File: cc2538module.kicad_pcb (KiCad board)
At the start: 4 copper layers, 24.4 x 27.6 mm, 68 parts, among them J1 XBEE_with_jtag, SW1 SW_PUSH, SW2 SW_PUSH, U1 CC2538, U2 TPS6273X, Y1 Crystal_GND24, Y2 Crystal

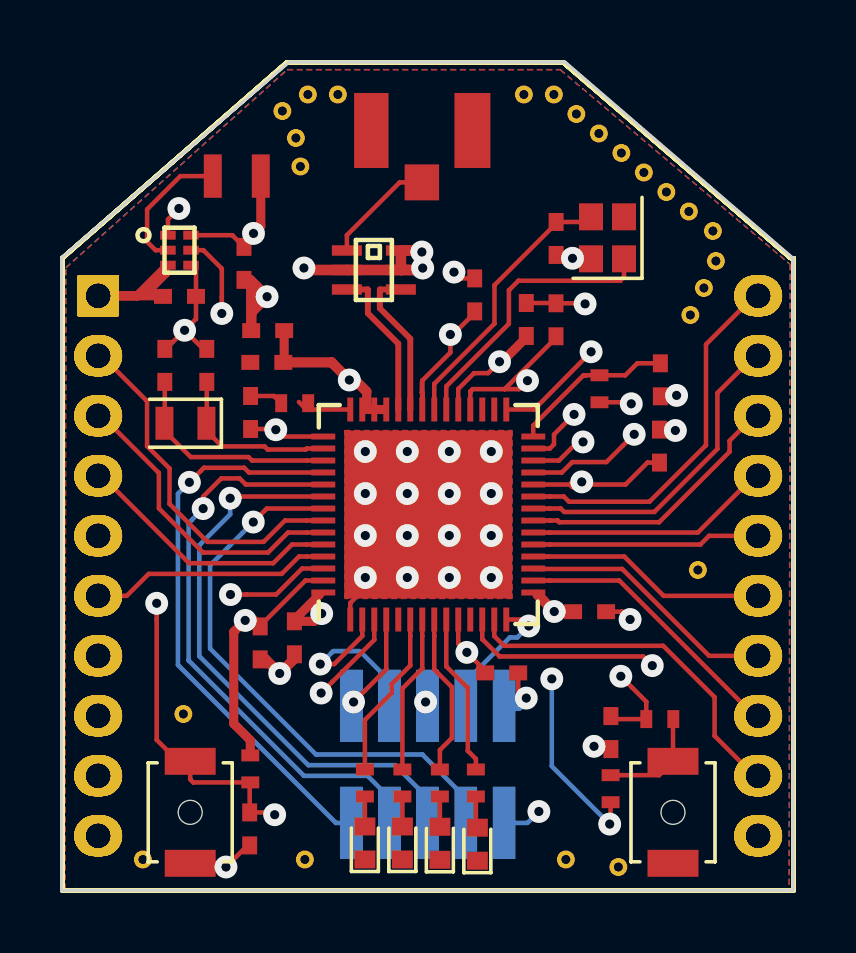
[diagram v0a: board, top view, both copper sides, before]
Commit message: Added C5 to PCB and rearrange the step down power converter as described in its datasheet
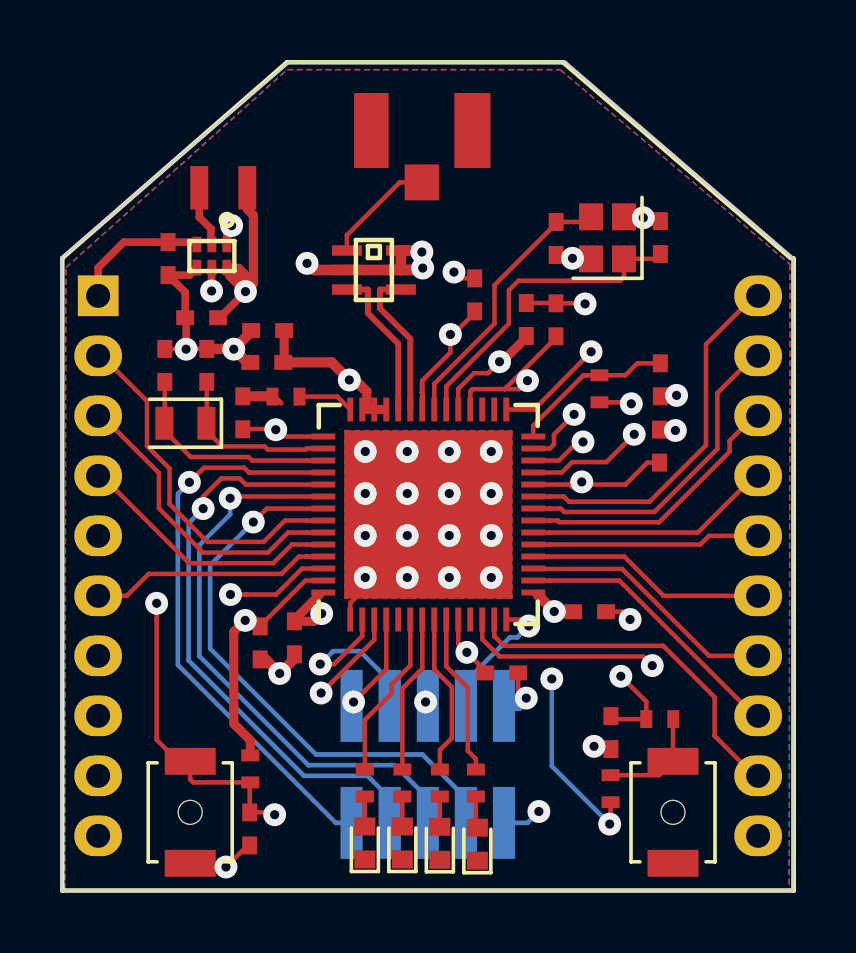
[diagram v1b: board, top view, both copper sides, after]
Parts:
- removed the J1 at (90.6, 65.1) (x3)
- removed REF** (x23): VIA-0.6mm, SensorsUnleashed:VIA-0.6mm
- added C5: 12pF, Capacitors_SMD:C_0402_NoSilk, F.Cu at (98.3, 57.1)
- C1: value 1n -> 1nF
- C13, C14, C16, C17, C18, C19: value 100n -> 100nF
- C2, C4: value 1u -> 1uF
- C20: value 220p -> 220pF
- C6: value 12p -> 12pF
- C8, C9: value 22p -> 22pF
- LED2: value Yellow -> Amber
- R2: value R -> 1k
- R6, R7, R8, R9: value 680R -> 100R
- moved C10 2.29 mm to (83.1, 59.8), turned to 180 degrees
- moved C11 1.32 mm to (81.9, 57.8), turned to 270 degrees
- moved U2 1.10 mm to (83.4, 57.7), turned to 270 degrees
- moved L1 0.60 mm to (83.8, 55.5)
- moved R3 0.36 mm to (85.9, 62.4)
- moved C18 0.26 mm to (84.4, 63.0)
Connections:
- net PA0/DIO0 renamed PA0/DIO7
- net PA1/DIO1 renamed PA1/DIO6
- net PA2/DIO2 renamed PA2/DIO5
- net PA3/DIO3 renamed PA3/DIO4
- net PA4/DIO4 renamed PA4/DIO3
- net PA5/DIO5 renamed PA5/DIO2
- net PA6/DIO6 renamed PA6/DIO1
- net PA7/DIO7 renamed PA7/DIO0
- net PB0/STAT renamed PD3/STAT
- net PC3/DIO10 renamed PD2/DIO10
- net PC4/L0 renamed PC7/L0
- net PC5/L1 renamed PC6/L1
- net PC6/L2 renamed PC5/L2
- net PC7/L3 renamed PC4/L3
- net USER_BUTTON renamed PD0/USER_BUTTON
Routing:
- net XBEE_VDD: track 7.84 -> 4.61 mm
- net Net-(L1-Pad1): track 4.54 -> 2.06 mm
- net VDD: track 89.8 -> 92.3 mm
- net PD3/STAT: track 20.4 -> 18.1 mm
- net GND: track 51.5 -> 53.0 mm, vias 31 -> 32
- net Net-(C5-Pad1): track 9.46 -> 10.7 mm
- net PB1/ON/BYP: track 17.0 -> 15.9 mm

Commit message: New footprint and various small changes. PCB ordered at DirtyPCB 20170328
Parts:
- added REF**: VIA-0.6mm, SensorsUnleashed:VIA-0.6mm, F.Cu at (87.9, 60.5)
- added REF**: VIA-0.6mm, SensorsUnleashed:VIA-0.6mm, F.Cu at (81.4, 78.3)
- added REF**: VIA-0.6mm, SensorsUnleashed:VIA-0.6mm, F.Cu at (86.7, 78.3)
- added REF**: VIA-0.6mm, SensorsUnleashed:VIA-0.6mm, F.Cu at (85.9, 78.3)
- added REF**: VIA-0.6mm, SensorsUnleashed:VIA-0.6mm, F.Cu at (85.1, 78.3)
- added REF**: VIA-0.6mm, SensorsUnleashed:VIA-0.6mm, F.Cu at (94.1, 78.3)
- added REF**: VIA-0.6mm, SensorsUnleashed:VIA-0.6mm, F.Cu at (94.9, 78.3)
- added REF**: VIA-0.6mm, SensorsUnleashed:VIA-0.6mm, F.Cu at (95.7, 78.3)
- added REF**: VIA-0.6mm, SensorsUnleashed:VIA-0.6mm, F.Cu at (96.5, 78.3)
- added REF**: VIA-0.6mm, SensorsUnleashed:VIA-0.6mm, F.Cu at (97.3, 78.3)
- added REF**: VIA-0.6mm, SensorsUnleashed:VIA-0.6mm, F.Cu at (95.6, 74.6)
- added REF**: VIA-0.6mm, SensorsUnleashed:VIA-0.6mm, F.Cu at (81.4, 72.7)
- added REF**: VIA-0.6mm, SensorsUnleashed:VIA-0.6mm, F.Cu at (99.8, 71.4)
- added REF**: VIA-0.6mm, SensorsUnleashed:VIA-0.6mm, F.Cu at (98.9, 61.2)
- added REF**: VIA-0.6mm, SensorsUnleashed:VIA-0.6mm, F.Cu at (86.5, 58.2)
- added REF**: VIA-0.6mm, SensorsUnleashed:VIA-0.6mm, F.Cu at (85.7, 58.2)
- added REF**: VIA-0.6mm, SensorsUnleashed:VIA-0.6mm, F.Cu at (85.7, 56.5)
- added REF**: VIA-0.6mm, SensorsUnleashed:VIA-0.6mm, F.Cu at (85.5, 55.7)
- added REF**: VIA-0.6mm, SensorsUnleashed:VIA-0.6mm, F.Cu at (85.2, 55.0)
- added REF**: VIA-0.6mm, SensorsUnleashed:VIA-0.6mm, F.Cu at (84.8, 54.3)
- added REF**: VIA-0.6mm, SensorsUnleashed:VIA-0.6mm, F.Cu at (83.7, 54.1)
- added REF**: VIA-0.6mm, SensorsUnleashed:VIA-0.6mm, F.Cu at (84.4, 53.6)
- added REF**: VIA-0.6mm, SensorsUnleashed:VIA-0.6mm, F.Cu at (81.4, 73.5)
- added REF**: VIA-0.6mm, SensorsUnleashed:VIA-0.6mm, F.Cu at (85.0, 53.0)
- added REF**: VIA-0.6mm, SensorsUnleashed:VIA-0.6mm, F.Cu at (85.6, 52.5)
- added REF**: VIA-0.6mm, SensorsUnleashed:VIA-0.6mm, F.Cu at (99.0, 60.4)
- added REF**: VIA-0.6mm, SensorsUnleashed:VIA-0.6mm, F.Cu at (99.5, 59.8)
- added REF**: VIA-0.6mm, SensorsUnleashed:VIA-0.6mm, F.Cu at (100.0, 59.3)
- added REF**: VIA-0.6mm, SensorsUnleashed:VIA-0.6mm, F.Cu at (100.1, 58.5)
- added REF**: VIA-0.6mm, SensorsUnleashed:VIA-0.6mm, F.Cu at (100.6, 57.9)
- added REF**: VIA-0.6mm, SensorsUnleashed:VIA-0.6mm, F.Cu at (101.4, 57.6)
- added REF**: VIA-0.6mm, SensorsUnleashed:VIA-0.6mm, F.Cu at (100.8, 57.1)
- added REF**: VIA-0.6mm, SensorsUnleashed:VIA-0.6mm, F.Cu at (100.2, 56.6)
- added REF**: VIA-0.6mm, SensorsUnleashed:VIA-0.6mm, F.Cu at (81.4, 75.9)
- added REF**: VIA-0.6mm, SensorsUnleashed:VIA-0.6mm, F.Cu at (99.6, 56.1)
- added REF**: VIA-0.6mm, SensorsUnleashed:VIA-0.6mm, F.Cu at (99.0, 55.6)
- added REF**: VIA-0.6mm, SensorsUnleashed:VIA-0.6mm, F.Cu at (98.4, 55.1)
- added REF**: VIA-0.6mm, SensorsUnleashed:VIA-0.6mm, F.Cu at (97.8, 54.6)
- added REF**: VIA-0.6mm, SensorsUnleashed:VIA-0.6mm, F.Cu at (97.2, 54.1)
- added REF**: VIA-0.6mm, SensorsUnleashed:VIA-0.6mm, F.Cu at (96.6, 53.6)
- added REF**: VIA-0.6mm, SensorsUnleashed:VIA-0.6mm, F.Cu at (96.0, 53.1)
- added REF**: VIA-0.6mm, SensorsUnleashed:VIA-0.6mm, F.Cu at (95.4, 52.6)
- added REF**: VIA-0.6mm, SensorsUnleashed:VIA-0.6mm, F.Cu at (94.8, 52.0)
- added REF**: VIA-0.6mm, SensorsUnleashed:VIA-0.6mm, F.Cu at (94.1, 52.0)
- added REF**: VIA-0.6mm, SensorsUnleashed:VIA-0.6mm, F.Cu at (81.4, 76.7)
- added REF**: VIA-0.6mm, SensorsUnleashed:VIA-0.6mm, F.Cu at (93.3, 52.0)
- added REF**: VIA-0.6mm, SensorsUnleashed:VIA-0.6mm, F.Cu at (91.2, 52.0)
- added REF**: VIA-0.6mm, SensorsUnleashed:VIA-0.6mm, F.Cu at (90.4, 52.0)
- added REF**: VIA-0.6mm, SensorsUnleashed:VIA-0.6mm, F.Cu at (89.6, 52.0)
- added REF**: VIA-0.6mm, SensorsUnleashed:VIA-0.6mm, F.Cu at (87.8, 52.0)
- added REF**: VIA-0.6mm, SensorsUnleashed:VIA-0.6mm, F.Cu at (87.0, 52.0)
- added REF**: VIA-0.6mm, SensorsUnleashed:VIA-0.6mm, F.Cu at (86.2, 52.0)
- added REF**: VIA-0.6mm, SensorsUnleashed:VIA-0.6mm, F.Cu at (81.4, 77.5)
- added REF**: VIA-0.6mm, SensorsUnleashed:VIA-0.6mm, F.Cu at (79.0, 78.3)
- added REF**: VIA-0.6mm, SensorsUnleashed:VIA-0.6mm, F.Cu at (79.8, 78.3)
- added REF**: VIA-0.6mm, SensorsUnleashed:VIA-0.6mm, F.Cu at (80.6, 78.3)
- U1: footprint Housings_DFN_QFN:QFN-56-1EP_7x7mm_Pitch0.4mm -> SensorsUnleashed:cc2538_QFN_56
- moved C14 2.05 mm to (96.9, 65.6), turned to 0 degrees
- moved C1 1.90 mm to (96.6, 61.1), turned to 0 degrees
- moved C17 1.04 mm to (91.5, 59.8)
- moved L1 0.77 mm to (83.1, 55.8)
- moved C12 0.70 mm to (92.5, 72.1), turned to 270 degrees
- moved C4 0.67 mm to (85.5, 70.6)
- moved TR1 0.64 mm to (89.0, 58.8)
- moved U2 0.57 mm to (82.8, 57.7)
- moved R3 0.57 mm to (85.6, 61.9)
- moved C15 0.54 mm to (84.5, 70.6)
- moved C18 0.53 mm to (84.2, 62.5)
- moved C20 0.52 mm to (85.3, 60.8)
- moved C11 0.50 mm to (81.5, 58.0)
- moved C19 0.43 mm to (85.3, 59.8)
- moved C13 0.35 mm to (96.3, 69.7)
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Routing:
- net GND: track 53.0 -> 76.6 mm, vias 32 -> 31
- net VDD: track 92.3 -> 100.6 mm, vias 11 -> 10
- net TCK: track 19.4 -> 22.6 mm
- net Net-(C1-Pad1): track 5.46 -> 2.99 mm
- net PD3/STAT: track 18.1 -> 15.9 mm
- net PD1/DIO11: track 29.3 -> 31.5 mm
- net RF_N: track 5.12 -> 3.66 mm
- net RF_P: track 5.12 -> 3.69 mm
- net USB_N: track 7.10 -> 8.13 mm
- net PC1/DIO8: track 12.0 -> 11.2 mm
- net PB3/DIO13: track 8.97 -> 8.11 mm
- net Net-(C8-Pad1): track 5.80 -> 5.06 mm
- net Net-(AE1-Pad1): track 3.74 -> 4.35 mm
- net Net-(C9-Pad1): track 7.34 -> 6.73 mm
- net XBEE_VDD: track 4.61 -> 4.01 mm
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
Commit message: Rev B
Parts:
- removed C10, C11: 2.2uF, Capacitors_SMD:C_0402_NoSilk
- removed L1: 2.2uH, SensorsUnleashed:L_0805
- removed the REF** at (87.9, 60.5)
- removed the REF** at (81.4, 78.3)
- removed the REF** at (86.7, 78.3)
- removed the REF** at (85.9, 78.3)
- removed the REF** at (85.1, 78.3)
- removed the REF** at (94.1, 78.3)
- removed the REF** at (94.9, 78.3)
- removed the REF** at (95.7, 78.3)
- removed the REF** at (96.5, 78.3)
- removed the REF** at (97.3, 78.3)
- removed the REF** at (95.6, 74.6)
- removed the REF** at (81.4, 72.7)
- removed the REF** at (99.8, 71.4)
- removed the REF** at (98.9, 61.2)
- removed the REF** at (86.5, 58.2)
- removed the REF** at (85.7, 58.2)
- removed the REF** at (85.7, 56.5)
- removed the REF** at (85.5, 55.7)
- removed the REF** at (85.2, 55.0)
- removed the REF** at (84.8, 54.3)
- removed the REF** at (83.7, 54.1)
- removed the REF** at (84.4, 53.6)
- removed the REF** at (81.4, 73.5)
- removed the REF** at (85.0, 53.0)
- removed the REF** at (85.6, 52.5)
- removed the REF** at (99.0, 60.4)
- removed the REF** at (99.5, 59.8)
- removed the REF** at (100.0, 59.3)
- removed the REF** at (100.1, 58.5)
- removed the REF** at (100.6, 57.9)
- removed the REF** at (101.4, 57.6)
- removed the REF** at (100.8, 57.1)
- removed the REF** at (100.2, 56.6)
- removed the REF** at (81.4, 75.9)
- removed the REF** at (99.6, 56.1)
- removed the REF** at (99.0, 55.6)
- removed the REF** at (98.4, 55.1)
- removed the REF** at (97.8, 54.6)
- removed the REF** at (97.2, 54.1)
- removed the REF** at (96.6, 53.6)
- removed the REF** at (96.0, 53.1)
- removed the REF** at (95.4, 52.6)
- removed the REF** at (94.8, 52.0)
- removed the REF** at (94.1, 52.0)
- removed the REF** at (81.4, 76.7)
- removed the REF** at (93.3, 52.0)
- removed the REF** at (91.2, 52.0)
- removed the REF** at (90.4, 52.0)
- removed the REF** at (89.6, 52.0)
- removed the REF** at (87.8, 52.0)
- removed the REF** at (87.0, 52.0)
- removed the REF** at (86.2, 52.0)
- removed the REF** at (81.4, 77.5)
- removed the REF** at (79.0, 78.3)
- removed the REF** at (79.8, 78.3)
- removed the REF** at (80.6, 78.3)
- removed U2: TPS6273X, SensorsUnleashed:SON6
- added REF**: VIA-0.6mm, SensorsUnleashed:VIA-0.6mm, F.Cu at (87.3, 53.3)
- added REF**: VIA-0.6mm, SensorsUnleashed:VIA-0.6mm, F.Cu at (91.7, 56.9)
- added REF**: VIA-0.6mm, SensorsUnleashed:VIA-0.6mm, F.Cu at (101.0, 57.6)
- added REF**: VIA-0.6mm, SensorsUnleashed:VIA-0.6mm, F.Cu at (100.2, 56.8)
- added REF**: VIA-0.6mm, SensorsUnleashed:VIA-0.6mm, F.Cu at (99.3, 56.1)
- added REF**: VIA-0.6mm, SensorsUnleashed:VIA-0.6mm, F.Cu at (98.5, 55.3)
- added REF**: VIA-0.6mm, SensorsUnleashed:VIA-0.6mm, F.Cu at (97.6, 54.6)
- added REF**: VIA-0.6mm, SensorsUnleashed:VIA-0.6mm, F.Cu at (96.7, 53.8)
- added REF**: VIA-0.6mm, SensorsUnleashed:VIA-0.6mm, F.Cu at (95.9, 53.1)
- added REF**: VIA-0.6mm, SensorsUnleashed:VIA-0.6mm, F.Cu at (95.0, 52.4)
- added REF**: VIA-0.6mm, SensorsUnleashed:VIA-0.6mm, F.Cu at (93.9, 52.2)
- added REF**: VIA-0.6mm, SensorsUnleashed:VIA-0.6mm, F.Cu at (87.3, 54.6)
- added REF**: VIA-0.6mm, SensorsUnleashed:VIA-0.6mm, F.Cu at (92.8, 52.2)
- added REF**: VIA-0.6mm, SensorsUnleashed:VIA-0.6mm, F.Cu at (91.7, 52.2)
- added REF**: VIA-0.6mm, SensorsUnleashed:VIA-0.6mm, F.Cu at (90.6, 52.2)
- added REF**: VIA-0.6mm, SensorsUnleashed:VIA-0.6mm, F.Cu at (89.5, 52.2)
- added REF**: VIA-0.6mm, SensorsUnleashed:VIA-0.6mm, F.Cu at (88.4, 52.2)
- added REF**: VIA-0.6mm, SensorsUnleashed:VIA-0.6mm, F.Cu at (87.3, 52.2)
- added REF**: VIA-0.6mm, SensorsUnleashed:VIA-0.6mm, F.Cu at (86.2, 52.3)
- added REF**: VIA-0.6mm, SensorsUnleashed:VIA-0.6mm, F.Cu at (85.4, 53.0)
- added REF**: VIA-0.6mm, SensorsUnleashed:VIA-0.6mm, F.Cu at (84.5, 53.7)
- added REF**: VIA-0.6mm, SensorsUnleashed:VIA-0.6mm, F.Cu at (83.7, 54.5)
- added REF**: VIA-0.6mm, SensorsUnleashed:VIA-0.6mm, F.Cu at (87.3, 55.7)
- added REF**: VIA-0.6mm, SensorsUnleashed:VIA-0.6mm, F.Cu at (82.9, 55.2)
- added REF**: VIA-0.6mm, SensorsUnleashed:VIA-0.6mm, F.Cu at (82.1, 55.9)
- added REF**: VIA-0.6mm, SensorsUnleashed:VIA-0.6mm, F.Cu at (81.3, 56.6)
- added REF**: VIA-0.6mm, SensorsUnleashed:VIA-0.6mm, F.Cu at (80.5, 57.4)
- added REF**: VIA-0.6mm, SensorsUnleashed:VIA-0.6mm, F.Cu at (87.2, 56.9)
- added REF**: VIA-0.6mm, SensorsUnleashed:VIA-0.6mm, F.Cu at (87.2, 58.1)
- added REF**: VIA-0.6mm, SensorsUnleashed:VIA-0.6mm, F.Cu at (93.5, 53.2)
- added REF**: VIA-0.6mm, SensorsUnleashed:VIA-0.6mm, F.Cu at (93.5, 54.3)
- added REF**: VIA-0.6mm, SensorsUnleashed:VIA-0.6mm, F.Cu at (93.3, 55.4)
- added REF**: VIA-0.6mm, SensorsUnleashed:VIA-0.6mm, F.Cu at (92.3, 55.7)
- C1, C12, C13, C14, C15, C16, C17, C18, C19, C2, C20, C3, C4, C5, C6, C7, C8, C9: footprint Capacitors_SMD:C_0402_NoSilk -> Capacitor_SMD:C_0402_1005Metric
- LED1, LED2, LED3, LED4: footprint LEDs:LED_0402 -> LED_SMD:LED_0402_1005Metric
- R1, R2, R3, R4, R5, R6, R7, R8, R9: footprint Resistors_SMD:R_0402_NoSilk -> Resistor_SMD:R_0402_1005Metric
- SW1, SW2: footprint Buttons_Switches_SMD:SW_SPST_B3U-1000P-B -> Button_Switch_SMD:SW_SPST_B3U-1000P-B
- Y1: footprint Crystals:Crystal_SMD_2016-4pin_2.0x1.6mm -> Crystal:Crystal_SMD_2016-4Pin_2.0x1.6mm
- Y2: footprint Crystals:Crystal_SMD_2012-2pin_2.0x1.2mm -> Crystal:Crystal_SMD_2012-2Pin_2.0x1.2mm
- moved C7 4.01 mm to (95.2, 77.3)
- moved R5 2.79 mm to (96.4, 75.2), turned to 270 degrees
- moved C16 2.36 mm to (96.3, 59.5), turned to 0 degrees
- moved C20 2.08 mm to (87.3, 60.4), turned to 90 degrees
- moved R1 1.95 mm to (98.4, 61.4), turned to 90 degrees
- moved R3 1.82 mm to (84.7, 60.4), turned to 90 degrees
- moved C2 1.76 mm to (95.8, 61.4)
- moved R4 1.50 mm to (95.2, 75.2), turned to 90 degrees
- moved C15 1.50 mm to (84.3, 69.1), turned to 180 degrees
- moved C17 1.32 mm to (92.4, 58.9)
- moved C4 1.22 mm to (84.3, 70.4), turned to 180 degrees
- moved TR1 1.11 mm to (89.6, 57.9)
- moved C19 0.91 mm to (86.0, 60.4), turned to 90 degrees
- moved C13 0.67 mm to (97.0, 69.7)
- moved C3 0.67 mm to (85.1, 77.3)
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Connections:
- J1 pad 1: XBEE_VDD -> VDD
- U1 pad 29: PD3/STAT -> Net-(U1-Pad29)
- U1 pad 54: PB1/ON/BYP -> Net-(U1-Pad54)
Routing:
- net VDD: track 100.6 -> 34.2 mm, vias 10 -> 9
- net PD3/STAT: track 15.9 -> 0.00 mm, vias 2 -> 0
- net PB1/ON/BYP: track 15.4 -> 0.00 mm, vias 2 -> 0
- net GND: track 76.6 -> 62.9 mm, vias 31 -> 21
- net PD0/USER_BUTTON: track 16.3 -> 25.2 mm
- net NRST: track 40.6 -> 48.0 mm, vias 4 -> 3
- net XBEE_VDD: track 4.01 -> 0.00 mm
- net PD2/DIO10: track 31.6 -> 33.6 mm
- net Net-(L1-Pad1): track 1.73 -> 0.00 mm
- net Net-(AE1-Pad1): track 4.35 -> 2.63 mm
- net Net-(R3-Pad1): track 1.65 -> 3.33 mm
- net PB6/TDI: track 19.2 -> 17.8 mm
- net Net-(C1-Pad1): track 2.99 -> 4.32 mm
- net Net-(C2-Pad1): track 20.6 -> 21.6 mm
- net PD1/DIO11: track 31.5 -> 30.5 mm
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- added copper zone on In2.Cu, net VDD
- removed copper zone on In2.Cu, net GND
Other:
- board text added: "Sensors Unleashed Radio One - rev. B www.sensorsunleashed.com"
- board text removed: "Sensors Unleashed Radio One - rev. A www.sensorsunleashed.com"
